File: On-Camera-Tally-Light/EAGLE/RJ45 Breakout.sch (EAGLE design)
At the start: 6 parts, among them J1 MAGJACK

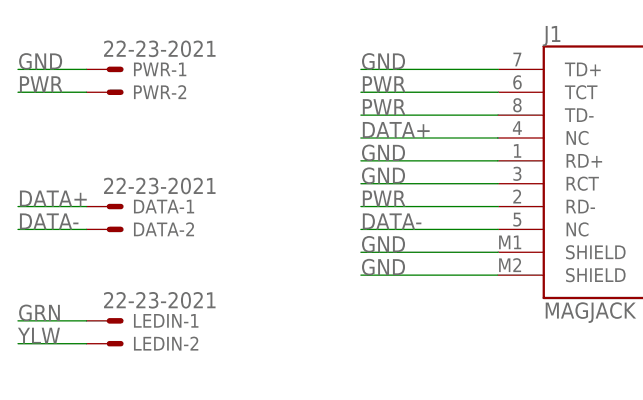
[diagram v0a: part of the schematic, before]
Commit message: Standardize RS485 pinouts, update RJ45 pinouts.
Fix pin assignments for the RS485 interconnects to standardize on pin1 = data-.
Update the RJ45 breakouts to be mostly pin compatible with DMX over ethernet wiring standard (using pin 5/6 for V+)
Create an XLR RS485 breakout option for wiring cameras together using 3pin DMX cables
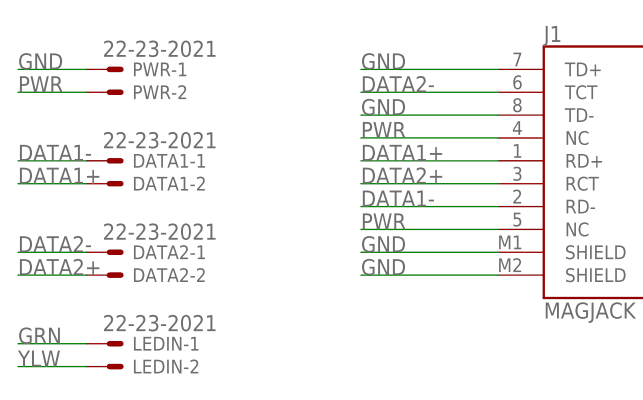
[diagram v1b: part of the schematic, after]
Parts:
- removed DATA: 22-23-2021, con-molex:22-23-2021
- added DATA1, DATA2: 22-23-2021, con-molex:22-23-2021
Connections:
- removed net DATA+: DATA-1.S, J1.NC@4
- removed net DATA-: DATA-2.S, J1.NC@5
- new net DATA1+: DATA1-2.S, J1.RD+
- new net DATA1-: DATA1-1.S, J1.RD-
- new net DATA2+: DATA2-2.S, J1.RCT
- new net DATA2-: DATA2-1.S, J1.TCT
- net GND: now also J1.TD-; no longer J1.RCT, J1.RD+
- net PWR: now also J1.NC@4, J1.NC@5; no longer J1.RD-, J1.TCT, J1.TD-
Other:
- moved on the sheet: LEDIN-1, LEDIN-2
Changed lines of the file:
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@@
 </classes>
 <parts>
-<part name="DATA" library="con-molex" library_urn="urn:adsk.eagle:library:165" deviceset="22-23-2021" device="" package3d_urn="urn:adsk.eagle:package:8078633/1"/>
+<part name="DATA1" library="con-molex" library_urn="urn:adsk.eagle:library:165" deviceset="22-23-2021" device="" package3d_urn="urn:adsk.eagle:package:8078633/1"/>
 <part name="J1" library="SparkFun-Connectors" library_urn="urn:adsk.eagle:library:513" deviceset="MAGJACK" device="" package3d_urn="urn:adsk.eagle:package:38215/1"/>
 <part name="PWR" library="con-molex" library_urn="urn:adsk.eagle:library:165" deviceset="22-23-2021" device="" package3d_urn="urn:adsk.eagle:package:8078633/1"/>
@@
 <part name="R1" library="rcl" library_urn="urn:adsk.eagle:library:334" deviceset="R-US_" device="0207/10" package3d_urn="urn:adsk.eagle:package:23491/2"/>
 <part name="R2" library="rcl" library_urn="urn:adsk.eagle:library:334" deviceset="R-US_" device="0207/10" package3d_urn="urn:adsk.eagle:package:23491/2"/>
+<part name="DATA2" library="con-molex" library_urn="urn:adsk.eagle:library:165" deviceset="22-23-2021" device="" package3d_urn="urn:adsk.eagle:package:8078633/1"/>
 </parts>
 <sheets>
@@
 </plain>
 <instances>
-<instance part="DATA" gate="-1" x="43.18" y="78.74" smashed="yes">
-<attribute name="NAME" x="45.72" y="77.978" size="1.524" layer="95"/>
-<attribute name="VALUE" x="42.418" y="80.137" size="1.778" layer="96"/>
-</instance>
-<instance part="DATA" gate="-2" x="43.18" y="76.2" smashed="yes">
-<attribute name="NAME" x="45.72" y="75.438" size="1.524" layer="95"/>
+<instance part="DATA1" gate="-1" x="43.18" y="83.82" smashed="yes">
+<attribute name="NAME" x="45.72" y="83.058" size="1.524" layer="95"/>
+<attribute name="VALUE" x="42.418" y="85.217" size="1.778" layer="96"/>
+</instance>
+<instance part="DATA1" gate="-2" x="43.18" y="81.28" smashed="yes">
+<attribute name="NAME" x="45.72" y="80.518" size="1.524" layer="95"/>
 </instance>
 <instance part="J1" gate="G$1" x="104.14" y="83.82" smashed="yes">
@@
 <attribute name="NAME" x="45.72" y="90.678" size="1.524" layer="95"/>
 </instance>
-<instance part="LEDIN" gate="-1" x="43.18" y="66.04" smashed="yes">
-<attribute name="NAME" x="45.72" y="65.278" size="1.524" layer="95"/>
-<attribute name="VALUE" x="42.418" y="67.437" size="1.778" layer="96"/>
-</instance>
-<instance part="LEDIN" gate="-2" x="43.18" y="63.5" smashed="yes">
+<instance part="LEDIN" gate="-1" x="43.18" y="63.5" smashed="yes">
 <attribute name="NAME" x="45.72" y="62.738" size="1.524" layer="95"/>
+<attribute name="VALUE" x="42.418" y="64.897" size="1.778" layer="96"/>
+</instance>
+<instance part="LEDIN" gate="-2" x="43.18" y="60.96" smashed="yes">
+<attribute name="NAME" x="45.72" y="60.198" size="1.524" layer="95"/>
 </instance>
 <instance part="FRAME1" gate="G$1" x="0" y="0" smashed="yes"/>
@@
 <attribute name="VALUE" x="125.73" y="90.678" size="1.778" layer="96"/>
 </instance>
+<instance part="DATA2" gate="-1" x="43.18" y="73.66" smashed="yes">
+<attribute name="NAME" x="45.72" y="72.898" size="1.524" layer="95"/>
+<attribute name="VALUE" x="42.418" y="75.057" size="1.778" layer="96"/>
+</instance>
+<instance part="DATA2" gate="-2" x="43.18" y="71.12" smashed="yes">
+<attribute name="NAME" x="45.72" y="70.358" size="1.524" layer="95"/>
+</instance>
 </instances>
 <busses>
 </busses>
 <nets>
-<net name="DATA-" class="0">
-<segment>
-<pinref part="DATA" gate="-2" pin="S"/>
-<wire x1="40.64" y1="76.2" x2="33.02" y2="76.2" width="0.1524" layer="91"/>
-<label x="33.02" y="76.2" size="1.778" layer="95"/>
-</segment>
-<segment>
-<pinref part="J1" gate="G$1" pin="NC@5"/>
-<wire x1="86.36" y1="76.2" x2="71.12" y2="76.2" width="0.1524" layer="91"/>
-<label x="71.12" y="76.2" size="1.778" layer="95"/>
-</segment>
-</net>
-<net name="DATA+" class="0">
-<segment>
-<pinref part="DATA" gate="-1" pin="S"/>
-<wire x1="40.64" y1="78.74" x2="33.02" y2="78.74" width="0.1524" layer="91"/>
-<label x="33.02" y="78.74" size="1.778" layer="95"/>
-</segment>
-<segment>
-<pinref part="J1" gate="G$1" pin="NC@4"/>
-<wire x1="86.36" y1="86.36" x2="71.12" y2="86.36" width="0.1524" layer="91"/>
-<label x="71.12" y="86.36" size="1.778" layer="95"/>
-</segment>
-</net>
 <net name="GND" class="0">
 <segment>
@@
 </segment>
 <segment>
-<pinref part="J1" gate="G$1" pin="RD+"/>
-<wire x1="86.36" y1="83.82" x2="71.12" y2="83.82" width="0.1524" layer="91"/>
-<label x="71.12" y="83.82" size="1.778" layer="95"/>
-</segment>
-<segment>
-<pinref part="J1" gate="G$1" pin="RCT"/>
-<wire x1="86.36" y1="81.28" x2="71.12" y2="81.28" width="0.1524" layer="91"/>
-<label x="71.12" y="81.28" size="1.778" layer="95"/>
-</segment>
-<segment>
 <pinref part="J1" gate="G$1" pin="TD+"/>
 <wire x1="86.36" y1="93.98" x2="71.12" y2="93.98" width="0.1524" layer="91"/>
 <label x="71.12" y="93.98" size="1.778" layer="95"/>
 </segment>
+<segment>
+<pinref part="J1" gate="G$1" pin="TD-"/>
+<wire x1="86.36" y1="88.9" x2="71.12" y2="88.9" width="0.1524" layer="91"/>
+<label x="71.12" y="88.9" size="1.778" layer="95"/>
+</segment>
 </net>
 <net name="GRN" class="0">
 <segment>
 <pinref part="LEDIN" gate="-1" pin="S"/>
-<wire x1="40.64" y1="66.04" x2="33.02" y2="66.04" width="0.1524" layer="91"/>
-<label x="33.02" y="66.04" size="1.778" layer="95"/>
+<wire x1="40.64" y1="63.5" x2="33.02" y2="63.5" width="0.1524" layer="91"/>
+<label x="33.02" y="63.5" size="1.778" layer="95"/>
 </segment>
 <segment>
@@
 <segment>
 <pinref part="LEDIN" gate="-2" pin="S"/>
-<wire x1="40.64" y1="63.5" x2="33.02" y2="63.5" width="0.1524" layer="91"/>
-<label x="33.02" y="63.5" size="1.778" layer="95"/>
+<wire x1="40.64" y1="60.96" x2="33.02" y2="60.96" width="0.1524" layer="91"/>
+<label x="33.02" y="60.96" size="1.778" layer="95"/>
 </segment>
 <segment>
@@
 </segment>
 <segment>
+<pinref part="J1" gate="G$1" pin="NC@4"/>
+<wire x1="86.36" y1="86.36" x2="71.12" y2="86.36" width="0.1524" layer="91"/>
+<label x="71.12" y="86.36" size="1.778" layer="95"/>
+</segment>
+<segment>
+<pinref part="J1" gate="G$1" pin="NC@5"/>
+<wire x1="86.36" y1="76.2" x2="71.12" y2="76.2" width="0.1524" layer="91"/>
+<label x="71.12" y="76.2" size="1.778" layer="95"/>
+</segment>
+</net>
+<net name="DATA2-" class="0">
+<segment>
 <pinref part="J1" gate="G$1" pin="TCT"/>
 <wire x1="86.36" y1="91.44" x2="71.12" y2="91.44" width="0.1524" layer="91"/>
@@
 </segment>
 <segment>
-<pinref part="J1" gate="G$1" pin="TD-"/>
-<wire x1="86.36" y1="88.9" x2="71.12" y2="88.9" width="0.1524" layer="91"/>
-<label x="71.12" y="88.9" size="1.778" layer="95"/>
-</segment>
+<pinref part="DATA2" gate="-1" pin="S"/>
+<wire x1="40.64" y1="73.66" x2="33.02" y2="73.66" width="0.1524" layer="91"/>
+<label x="33.02" y="73.66" size="1.778" layer="95"/>
+</segment>
+</net>
+<net name="DATA1+" class="0">
+<segment>
+<pinref part="J1" gate="G$1" pin="RD+"/>
+<wire x1="86.36" y1="83.82" x2="71.12" y2="83.82" width="0.1524" layer="91"/>
+<label x="71.12" y="83.82" size="1.778" layer="95"/>
+</segment>
+<segment>
+<pinref part="DATA1" gate="-2" pin="S"/>
+<wire x1="40.64" y1="81.28" x2="33.02" y2="81.28" width="0.1524" layer="91"/>
+<label x="33.02" y="81.28" size="1.778" layer="95"/>
+</segment>
+</net>
+<net name="DATA2+" class="0">
+<segment>
+<pinref part="J1" gate="G$1" pin="RCT"/>
+<wire x1="86.36" y1="81.28" x2="71.12" y2="81.28" width="0.1524" layer="91"/>
+<label x="71.12" y="81.28" size="1.778" layer="95"/>
+</segment>
+<segment>
+<pinref part="DATA2" gate="-2" pin="S"/>
+<wire x1="40.64" y1="71.12" x2="33.02" y2="71.12" width="0.1524" layer="91"/>
+<label x="33.02" y="71.12" size="1.778" layer="95"/>
+</segment>
+</net>
+<net name="DATA1-" class="0">
 <segment>
 <pinref part="J1" gate="G$1" pin="RD-"/>
@@
 <label x="71.12" y="78.74" size="1.778" layer="95"/>
 </segment>
-</net>
+<segment>
+<pinref part="DATA1" gate="-1" pin="S"/>
+<wire x1="40.64" y1="83.82" x2="33.02" y2="83.82" width="0.1524" layer="91"/>
+<label x="33.02" y="83.82" size="1.778" layer="95"/>
+</segment>
+</net>

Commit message: Update RJ45 boards to use RJHSE Amphenol jacks
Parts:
- J1: value MAGJACK -> RJHSE-5381; device SparkFun-Connectors:MAGJACK -> RJHSE-5381:RJHSE-5381
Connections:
- removed net GRN: LEDIN-1.S, R1.2
- removed net GRNIN: J1.GLED+, R1.1
- removed net PWR: J1.NC@4, J1.NC@5, PWR-2.S
- removed net YLW: LEDIN-2.S, R2.2
- removed net YLWIN: J1.YLED+, R2.1
- new net LED1: J1.10, R1.2
- new net LED1IN: LEDIN-1.S, R1.1
- new net LED2: J1.12, R2.2
- new net LED2IN: LEDIN-2.S, R2.1
- new net VCC: J1.4, J1.5, PWR-2.S
- net DATA1+: now also J1.1; no longer J1.RD+
- net DATA1-: now also J1.2; no longer J1.RD-
- net DATA2+: now also J1.3; no longer J1.RCT
- net DATA2-: now also J1.6; no longer J1.TCT
- net GND: now also J1.11, J1.7, J1.8, J1.9, J1.S1, J1.S2; no longer J1.GLED-, J1.SHIELD@0, J1.SHIELD@1, J1.TD+, J1.TD-, J1.YLED-
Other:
- moved on the sheet: R1, R2
